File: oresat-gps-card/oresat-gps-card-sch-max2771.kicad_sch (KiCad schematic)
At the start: 78 parts, among them U12 7Q-16.368MBG-T, U13 MAX2769, U20 MAX2769ETI+, U21 LT1719S6, U22 XC2C64A-5VQG44C, U24 D32G-016.368M, U26 LT1719IS6, U28 LT1719IS6

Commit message: Routine Push
Andrew should look at the MAX2769 change.
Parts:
- added C?: 100p, Capacitor_SMD:C_0603_1608Metric, symbol Device:C
- added C?: 100n, Capacitor_SMD:C_0603_1608Metric, symbol Device:C
- added R?: 1k, Resistor_SMD:R_0603_1608Metric, symbol Device:R_US
- added R?: 10k, Resistor_SMD:R_0603_1608Metric, symbol Device:R_US
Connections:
- net CPOUT is gone; now on an unnamed net: C92.2, R81.2
- net GND: now also U13.29 (GND), C?.2, C?.2, R?.1, R?.2
- net LNAOUT: no longer FL2.1
- net MAX_SPI1_CS0: now also R88.1, U13.7 (~{SHDN}); no longer R86.2, U13.10 (~{CS})
- net MAX_~{SHDN}: now also R86.2, U13.10 (~{CS}); no longer R88.1, U13.7 (~{SHDN})
- net MIXIN: no longer FL2.4
- net at U13.15 (XTAL): now also C88.2
- net at U13.2 (LNAOUT): now also FL2.1
- net at U13.24 (~{IDLE}): now also R?.2
- net at U13.26 (PGM): now also R?.1
- net at U13.3 (ANTBIAS): now also C?.1, C?.1
- net at U13.5 (MIXIN): now also FL2.4
- no-connect marks 0 -> 4
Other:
- moved on the sheet: C100, C74, C79, C81, C84, C86, C88, C92, C94, FL2, L4, R81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

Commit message: Routine Push
First attempt to clean up schematic
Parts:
- removed C51, C52, C55, C60, C64, C66, C68, C70, C72, C73, C80, C82, C83, C85: 100n, v3-gps:.0402-C-NOSILK, symbol v3-gps-eagle-import:C-EU0402-C-NOSILK
- removed C53, C58: 2.2u, v3-gps:.0603-B-NOSILK, symbol v3-gps-eagle-import:C-EU0603-B-NOSILK
- removed C54, C57, C59, C61, C62, C63, C69, C71: 100p, v3-gps:.0402-C-NOSILK, symbol v3-gps-eagle-import:C-EU0402-C-NOSILK
- removed C56: 10n, v3-gps:.0402-C-NOSILK, symbol v3-gps-eagle-import:C-EU0402-C-NOSILK
- removed C65: 27p, v3-gps:.0402-C-NOSILK, symbol v3-gps-eagle-import:C-EU0402-C-NOSILK
- removed C67: 470p, v3-gps:.0402-C-NOSILK, symbol v3-gps-eagle-import:C-EU0402-C-NOSILK
- removed JP1: PINHD-1X6, v3-gps:1X06, symbol v3-gps-eagle-import:PINHD-1X6
- removed L8: SF14-1575F5UU19, v3-gps:SAW_1.4X1.1, symbol v3-gps-eagle-import:SAW_1.4X1.1
- removed R49, R50, R51, R62, R63: 10k, v3-gps:0402-C-NOSILK@1, symbol v3-gps-eagle-import:R-US_0402-C-NOSILK
- removed R52: 1k, v3-gps:0402-C-NOSILK@1, symbol v3-gps-eagle-import:R-US_0402-C-NOSILK
- removed R61: 20k, v3-gps:0402-C-NOSILK@1, symbol v3-gps-eagle-import:R-US_0402-C-NOSILK
- removed TP100, TP101, TP102, TP103, TP98, TP99: TEST-POINT15MIL-TEST-POINT, v3-gps:15MIL-TEST-POINT, symbol v3-gps-eagle-import:TEST-POINT15MIL-TEST-POINT
- removed U12: 7Q-16.368MBG-T, v3-gps:TCX_7Q, symbol v3-gps-eagle-import:7Q-16.368MBG-T
- removed U20: MAX2769ETI+, v3-gps:90-0023, symbol v3-gps-eagle-import:MAX2769
- removed U21: LT1719S6, v3-gps:SOT23-6, symbol v3-gps-eagle-import:IC_COMP_W_SDSOT23-6
- removed U22: XC2C64A-5VQG44C, v3-gps:VQ44, symbol v3-gps-eagle-import:XC2C32A_VQ44_2
- gave numbers to parts that had none: 4

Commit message: Routine Push
Schematic finished. Components laid out, chasing ERCs.
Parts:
- renumbered U26 to U28
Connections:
- net at U13.25 (LNA2): now also L4.2
- net MAX-LD: now reaches U13.6 (LD)
- no-connect marks 4 -> 3
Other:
- moved on the sheet: C100, C84, C86, L4, U28A, U28B

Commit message: Routine Push
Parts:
- added D12: GREEN, LED_SMD:LED_0603_1608Metric, symbol Device:LED
- added R62: 10k, Resistor_SMD:R_0603_1608Metric, symbol Device:R_US
- C84, C86, C92, C94: footprint Capacitor_SMD:C_0402_1005Metric -> Capacitor_SMD:C_0603_1608Metric
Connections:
- net 2.85VA: now also R62.2
- net 2.85VD: no longer U24.4 (VDD)
- net GND: now also D12.1 (K); no longer U24.2 (GND)
- net at C88.1: no longer U24.3 (OUT)
- new net: D12.2 (A), R62.1
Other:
- note added: "All resistors are 0603 1% AEC-Q200 unless marked. All capacitors are 0603 AEC-Q200 Vw >= 16V X5R or better unless marked."

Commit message: Push for Layout review
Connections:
- net 2.85VD: now also U24.4 (VDD)
- net GND: now also U24.2 (GND)
- net at C88.1: now also U24.3 (OUT)
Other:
- moved on the sheet: U24
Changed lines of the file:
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@@
 	(symbol
 		(lib_id "oresat-ics:D32G-016.368M")
-		(at 276.86 160.02 0)
+		(at 276.86 158.75 0)
 		(mirror y)
 		(unit 1)
@@
 		(fields_autoplaced yes)
 		(property "Reference" "U24"
-			(at 276.86 151.13 0)
+			(at 276.86 149.86 0)
 			(show_name no)
 			(do_not_autoplace no)
@@
 		)
 		(property "Value" "D32G-016.368M"
-			(at 276.86 153.67 0)
+			(at 276.86 152.4 0)
 			(show_name no)
 			(do_not_autoplace no)
@@
 		)
 		(property "Footprint" "oresat-ics:U-Connor-Winfield-D32G-016368M"
-			(at 276.86 148.082 0)
+			(at 276.86 146.812 0)
 			(hide yes)
 			(show_name no)
@@
 		)
 		(property "Datasheet" "http://www.conwin.com/datasheets/tx/tx240.pdf"
-			(at 276.86 146.304 0)
+			(at 276.86 145.034 0)
 			(hide yes)
 			(show_name no)
@@
 		)
 		(property "Description" ""
-			(at 276.86 160.02 0)
+			(at 276.86 158.75 0)
 			(hide yes)
 			(show_name no)

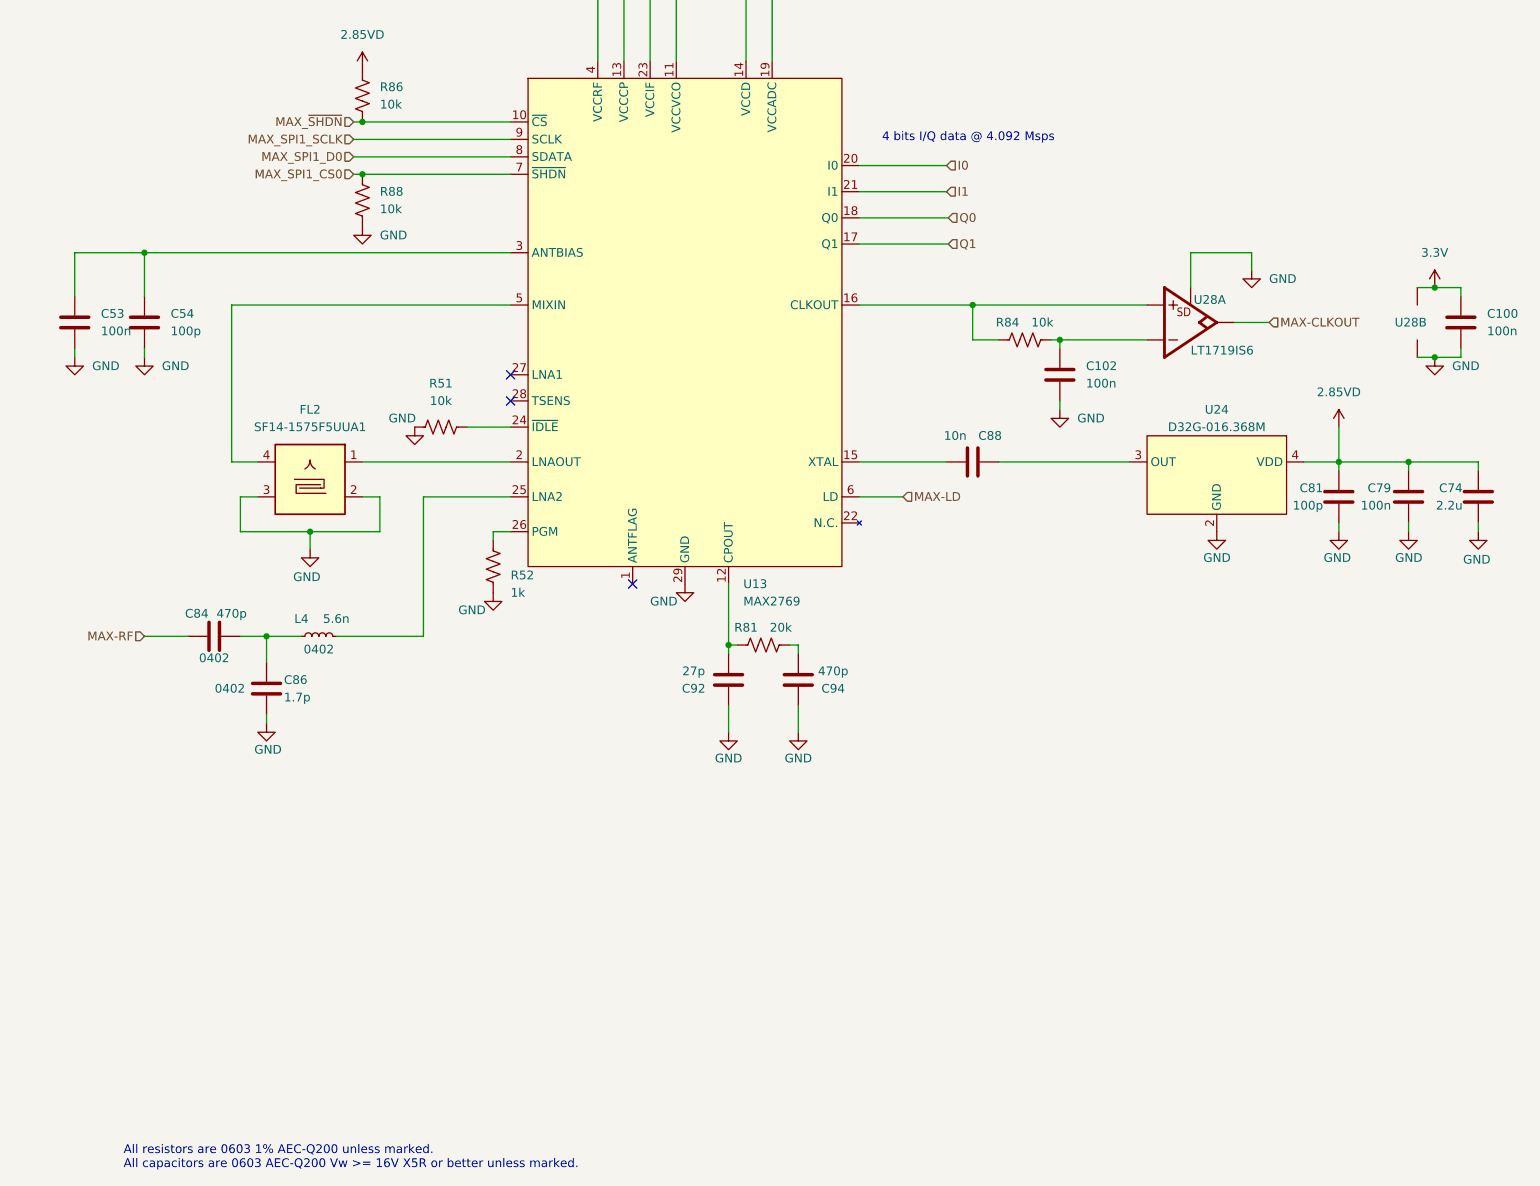
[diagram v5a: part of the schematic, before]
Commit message: General cleanup of schematic and layout
Updated .gitignore, updates DRU file, moved RF lines to RF-50-MIN (max is just too big),
lots of cleanup on the root page to make it pretty, cleaned up some redudant labels,
updated SMPM connector and added rule zone, updated PCB outline to include NPTH drills
for SMPM connectors, began cleanup of OPD.
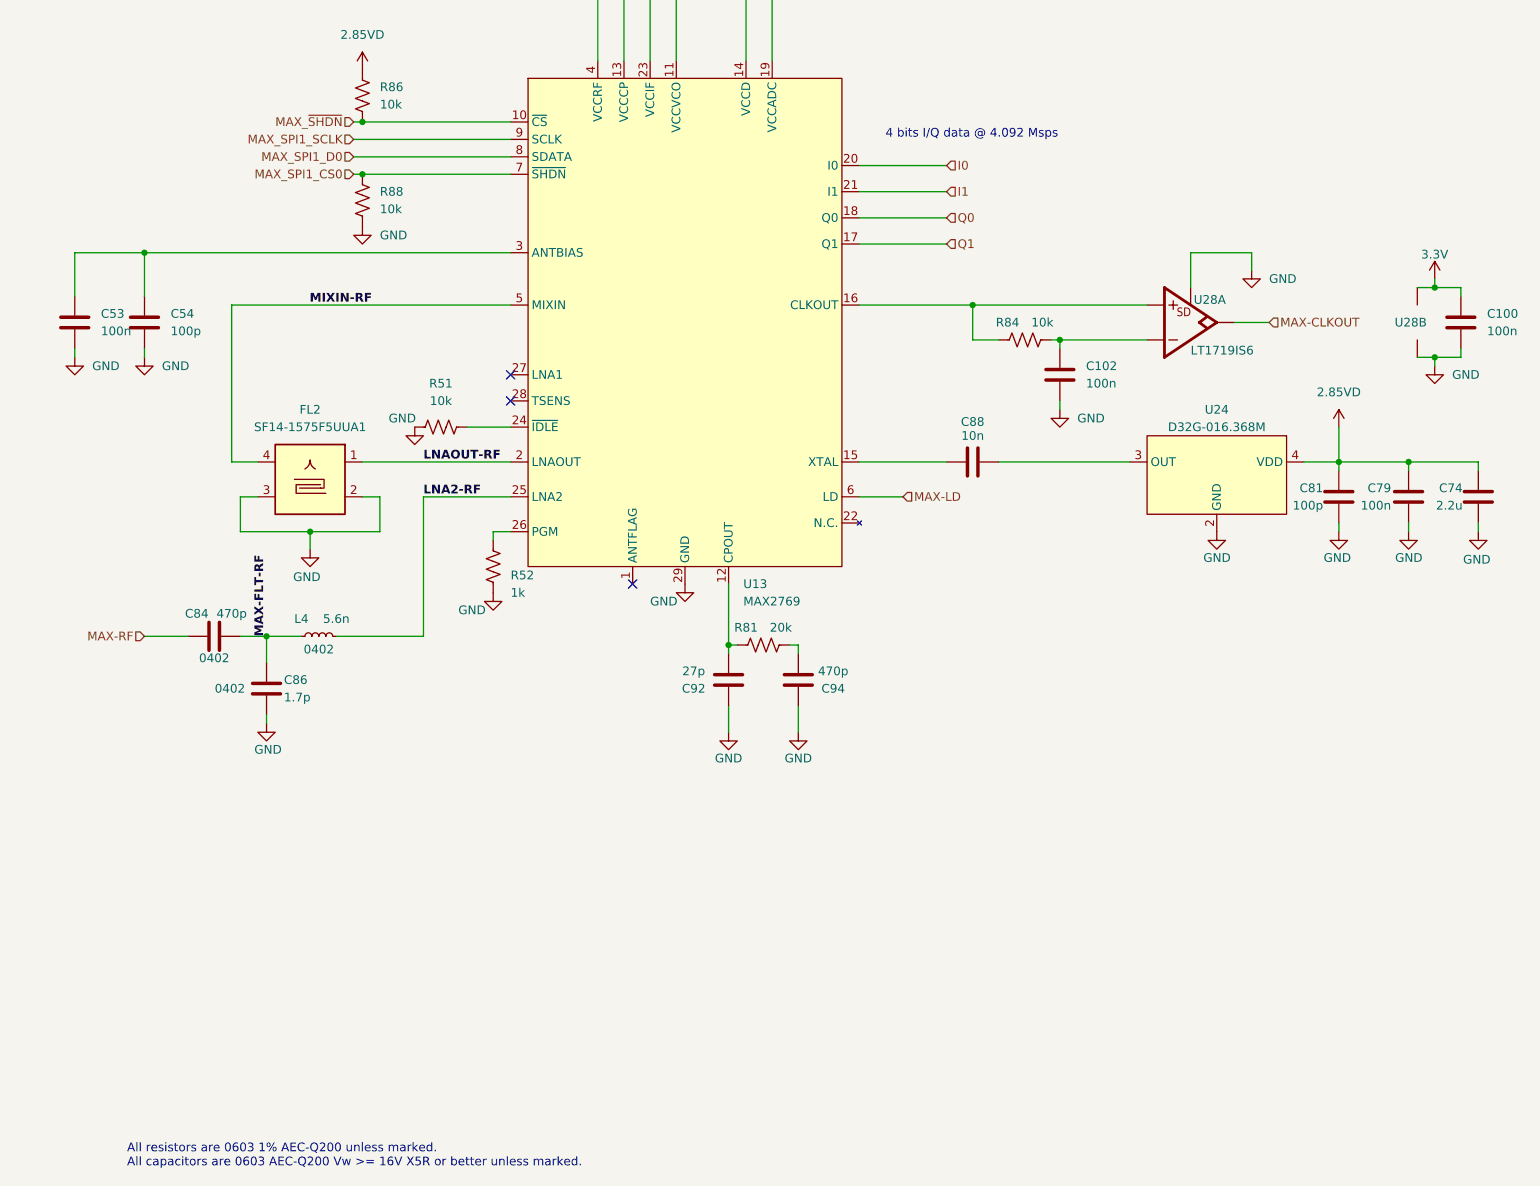
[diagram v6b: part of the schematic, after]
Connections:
- net LNAOUT-RF: now reaches FL2.1, U13.2 (LNAOUT)
- net MIXIN-RF: now reaches FL2.4, U13.5 (MIXIN)
- net MAX-FLT-RF: now reaches C84.2, C86.1, L4.1
- net LNA2-RF: now reaches L4.2, U13.25 (LNA2)
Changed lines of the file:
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@@
 	(text "All resistors are 0603 1% AEC-Q200 unless marked.\nAll capacitors are 0603 AEC-Q200 Vw >= 16V X5R or better unless marked."
 		(exclude_from_sim no)
-		(at 117.602 260.604 0)
+		(at 118.11 260.35 0)
 		(effects
 			(font
@@
 	(text "4 bits I/Q data @ 4.092 Msps"
 		(exclude_from_sim no)
-		(at 228.092 110.998 0)
+		(at 228.6 110.49 0)
 		(effects
 			(font
@@
 	)
 	(junction
-		(at 308.61 132.08)
-		(diameter 0)
-		(color 0 0 0 0)
-	)
-	(junction
 		(at 294.64 157.48)
 		(diameter 0)
@@
 	)
 	(junction
+		(at 308.61 132.08)
+		(diameter 0)
+		(color 0 0 0 0)
+	)
+	(junction
 		(at 152.4 107.95)
 		(diameter 0)
@@
 	(wire
 		(pts
+			(xy 308.61 143.51) (xy 308.61 142.24)
+		)
+		(stroke
+			(width 0)
+			(type default)
+		)
+	)
+	(wire
+		(pts
 			(xy 294.64 157.48) (xy 294.64 158.75)
 		)
@@
 	(wire
 		(pts
-			(xy 224.79 125.73) (xy 237.744 125.73)
+			(xy 224.79 125.73) (xy 237.49 125.73)
 		)
 		(stroke
@@
 	(wire
 		(pts
+			(xy 308.61 130.81) (xy 308.61 132.08)
+		)
+		(stroke
+			(width 0)
+			(type default)
+		)
+	)
+	(wire
+		(pts
 			(xy 217.17 63.5) (xy 217.17 60.96)
 		)
@@
 	(wire
 		(pts
-			(xy 224.79 121.92) (xy 237.744 121.92)
+			(xy 224.79 121.92) (xy 237.49 121.92)
 		)
 		(stroke
@@
 		)
 	)
+	(label "LNA2-RF"
+		(at 161.29 162.56 0)
+		(effects
+			(font
+				(size 1.27 1.27)
+				(thickness 0.254)
+				(bold yes)
+			)
+			(justify left bottom)
+		)
+	)
+	(label "MAX-FLT-RF"
+		(at 138.43 182.88 90)
+		(effects
+			(font
+				(size 1.27 1.27)
+				(thickness 0.254)
+				(bold yes)
+			)
+			(justify left bottom)
+		)
+	)
+	(label "LNAOUT-RF"
+		(at 161.29 157.48 0)
+		(effects
+			(font
+				(size 1.27 1.27)
+				(thickness 0.254)
+				(bold yes)
+			)
+			(justify left bottom)
+		)
+	)
+	(label "MIXIN-RF"
+		(at 144.7098 134.62 0)
+		(effects
+			(font
+				(size 1.27 1.27)
+				(thickness 0.254)
+				(bold yes)
+			)
+			(justify left bottom)
+		)
+	)
 	(hierarchical_label "Q0"
 		(shape input)
-		(at 237.744 121.92 0)
+		(at 237.49 121.92 0)
 		(effects
 			(font
@@
 	(hierarchical_label "Q1"
 		(shape input)
-		(at 237.744 125.73 0)
+		(at 237.49 125.73 0)
 		(effects
 			(font
@@
 		(dnp no)
 		(property "Reference" "C88"
-			(at 243.84 153.67 90)
+			(at 241.3 151.638 90)
 			(show_name no)
 			(do_not_autoplace no)
@@
 		)
 		(property "Value" "10n"
-			(at 238.76 153.67 90)
+			(at 241.3 153.67 90)
 			(show_name no)
 			(do_not_autoplace no)
@@
 	(symbol
 		(lib_id "power:GND")
-		(at 308.61 142.24 0)
+		(at 308.61 143.51 0)
 		(unit 1)
 		(body_style 1)
@@
 		(fields_autoplaced yes)
 		(property "Reference" "#GND0248"
-			(at 308.61 148.59 0)
+			(at 308.61 149.86 0)
 			(hide yes)
 			(show_name no)
@@
 		)
 		(property "Value" "GND"
-			(at 311.15 143.5099 0)
+			(at 311.15 144.7799 0)
 			(show_name no)
 			(do_not_autoplace no)
@@
 		)
 		(property "Footprint" ""
-			(at 308.61 142.24 0)
+			(at 308.61 143.51 0)
 			(hide yes)
 			(show_name no)
@@
 		)
 		(property "Datasheet" ""
-			(at 308.61 142.24 0)
+			(at 308.61 143.51 0)
 			(hide yes)
 			(show_name no)
@@
 		)
 		(property "Description" "Power symbol creates a global label with name \"GND\" , ground"
-			(at 308.61 142.24 0)
+			(at 308.61 143.51 0)
 			(hide yes)
 			(show_name no)
@@
 	(symbol
 		(lib_id "oresat-power:3.3V")
-		(at 308.61 132.08 0)
+		(at 308.61 130.81 0)
 		(unit 1)
 		(body_style 1)
@@
 		(in_pos_files yes)
 		(dnp no)
-		(fields_autoplaced yes)
 		(property "Reference" "#3V0115"
-			(at 308.61 135.89 0)
+			(at 308.61 134.62 0)
 			(hide yes)
 			(show_name no)
@@
 		)
 		(property "Value" "3.3V"
-			(at 308.61 127 0)
+			(at 308.61 127.254 0)
 			(show_name no)
 			(do_not_autoplace no)
@@
 		)
 		(property "Footprint" ""
-			(at 308.61 132.08 0)
+			(at 308.61 130.81 0)
 			(hide yes)
 			(show_name no)
@@
 		)
 		(property "Datasheet" ""
-			(at 308.61 132.08 0)
+			(at 308.61 130.81 0)
 			(hide yes)
 			(show_name no)
@@
 		)
 		(property "Description" ""
-			(at 308.61 132.08 0)
+			(at 308.61 130.81 0)
 			(hide yes)
 			(show_name no)
